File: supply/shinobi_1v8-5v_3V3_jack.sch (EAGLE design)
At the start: 19 parts, among them P1 POLYSWITCH1210

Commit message: Update.
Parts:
- added R6: 0, FaBo-Resistors:RESISTOR-0603-NARROW
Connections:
- net GND: now also R6.1
- net PS: now also R6.2
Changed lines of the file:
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@@
 <part name="VIN2" library="FaBo-Supply" deviceset="VIN" device=""/>
 <part name="VOUT3" library="FaBo-Supply" deviceset="VOUT" device=""/>
+<part name="R6" library="FaBo-Resistors" deviceset="RESISTOR" device="-0603-NARROW" value="0"/>
+<part name="GND12" library="FaBo-Supply" deviceset="GND" device=""/>
 </parts>
 <sheets>
@@
 <instance part="VIN2" gate="G$1" x="203.2" y="76.2"/>
 <instance part="VOUT3" gate="G$1" x="83.82" y="53.34"/>
+<instance part="R6" gate="G$1" x="73.66" y="116.84" rot="R90"/>
+<instance part="GND12" gate="G$1" x="73.66" y="106.68"/>
 </instances>
 <busses>
@@
 <wire x1="190.5" y1="134.62" x2="190.5" y2="93.98" width="0.1524" layer="91"/>
 </segment>
+<segment>
+<pinref part="GND12" gate="G$1" pin="GND"/>
+<pinref part="R6" gate="G$1" pin="1"/>
+<wire x1="73.66" y1="106.68" x2="73.66" y2="114.3" width="0.1524" layer="91"/>
+</segment>
 </net>
 <net name="N$3" class="0">
@@
 <pinref part="SJ2" gate="G$1" pin="2"/>
 <wire x1="73.66" y1="127" x2="73.66" y2="134.62" width="0.1524" layer="91"/>
-</segment>
-</net>
+<pinref part="R6" gate="G$1" pin="2"/>
+<wire x1="73.66" y1="121.92" x2="73.66" y2="127" width="0.1524" layer="91"/>
+</segment>
+</net>

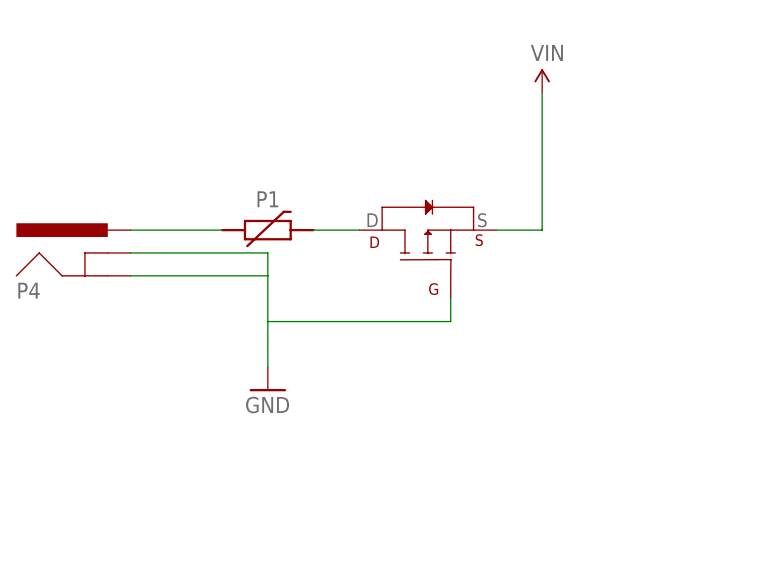
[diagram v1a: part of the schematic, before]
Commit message: Update 3v3.
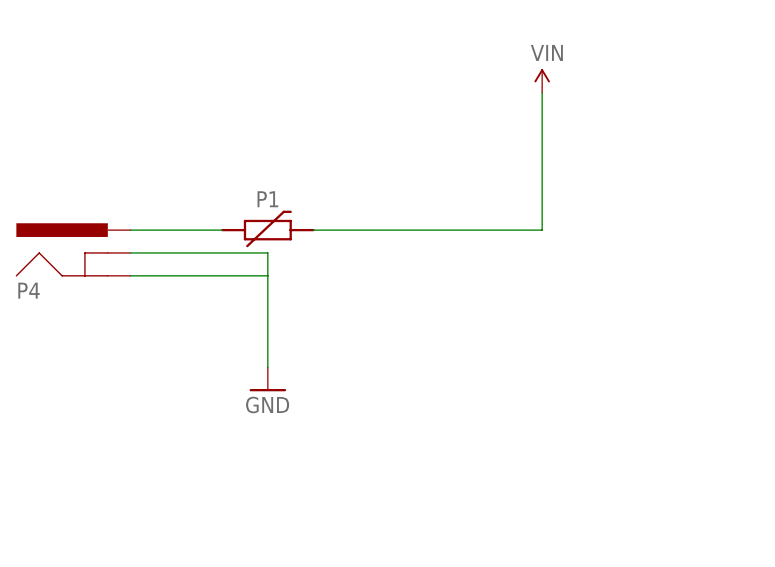
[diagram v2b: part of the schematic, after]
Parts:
- removed M1: (no value), FaBo-Transistor:AOD417
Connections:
- removed net N$15: M1.D, P1.2
- net GND: no longer M1.G
- net VIN: now also P1.2; no longer M1.S
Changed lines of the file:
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@@
 <?xml version="1.0" encoding="utf-8"?>
 <!DOCTYPE eagle SYSTEM "eagle.dtd">
-<eagle version="8.2.2">
+<eagle version="8.5.1">
 <drawing>
 <settings>
 <setting alwaysvectorfont="no"/>
+<setting keepoldvectorfont="yes"/>
 <setting verticaltext="up"/>
 </settings>
@@
 <part name="U$4" library="FaBo-etc" deviceset="A4L-LOC" device=""/>
 <part name="GND4" library="supply1" library_urn="urn:adsk.eagle:library:371" deviceset="GND" device=""/>
-<part name="M1" library="FaBo-Transistor" deviceset="AOD417" device=""/>
 <part name="P4" library="FaBo-Supply" deviceset="DC-JACK" device="MA04339A0"/>
 <part name="P1" library="FaBo-Supply" deviceset="POLYSWITCH" device="1210"/>
@@
 <instance part="U$4" gate="G$1" x="0" y="0"/>
 <instance part="GND4" gate="1" x="172.72" y="43.18"/>
-<instance part="M1" gate="G$1" x="190.5" y="60.96"/>
 <instance part="P4" gate="G$1" x="149.86" y="58.42"/>
 <instance part="P1" gate="G$1" x="172.72" y="60.96"/>
@@
 <pinref part="GND4" gate="1" pin="GND"/>
 <wire x1="172.72" y1="58.42" x2="172.72" y2="55.88" width="0.1524" layer="91"/>
-<wire x1="172.72" y1="55.88" x2="172.72" y2="50.8" width="0.1524" layer="91"/>
 <wire x1="157.48" y1="58.42" x2="172.72" y2="58.42" width="0.1524" layer="91"/>
 <wire x1="172.72" y1="55.88" x2="157.48" y2="55.88" width="0.1524" layer="91"/>
-<pinref part="M1" gate="G$1" pin="G"/>
-<wire x1="193.04" y1="53.34" x2="193.04" y2="50.8" width="0.1524" layer="91"/>
-<wire x1="193.04" y1="50.8" x2="172.72" y2="50.8" width="0.1524" layer="91"/>
-<wire x1="172.72" y1="50.8" x2="172.72" y2="45.72" width="0.1524" layer="91"/>
+<wire x1="172.72" y1="55.88" x2="172.72" y2="45.72" width="0.1524" layer="91"/>
 <pinref part="P4" gate="G$1" pin="GNDBREAK"/>
 <pinref part="P4" gate="G$1" pin="GND"/>
@@
 </segment>
 </net>
-<net name="N$15" class="0">
-<segment>
-<pinref part="M1" gate="G$1" pin="D"/>
-<wire x1="177.8" y1="60.96" x2="182.88" y2="60.96" width="0.1524" layer="91"/>
-<pinref part="P1" gate="G$1" pin="2"/>
-</segment>
-</net>
 <net name="FB" class="0">
 <segment>
@@
 </segment>
 <segment>
-<pinref part="M1" gate="G$1" pin="S"/>
-<wire x1="198.12" y1="60.96" x2="203.2" y2="60.96" width="0.1524" layer="91"/>
 <wire x1="203.2" y1="60.96" x2="203.2" y2="76.2" width="0.1524" layer="91"/>
 <pinref part="VIN2" gate="G$1" pin="VIN"/>
+<pinref part="P1" gate="G$1" pin="2"/>
+<wire x1="177.8" y1="60.96" x2="203.2" y2="60.96" width="0.1524" layer="91"/>
 </segment>
 </net>
@@
 <compatibility>
 <note version="8.2" severity="warning">
-Since Version 8.2, Eagle supports online libraries. The ids
+Since Version 8.2, EAGLE supports online libraries. The ids
 of those online libraries will not be understood (or retained)
 with this version.
